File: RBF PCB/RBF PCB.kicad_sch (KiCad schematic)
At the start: 0 parts

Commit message: schematic finished
schematic is finished and pending review
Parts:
- added J1, J2, J5, J6: DF11-12DP, Connector_Hirose:Hirose_DF11-12DP-2DSA_2x06_P2.00mm_Vertical, symbol Connector_Generic:Conn_02x06_Odd_Even
- added J3, J4, J7, J8: Conn_01x04_Pin, Connector_PinSocket_2.54mm:PinSocket_1x04_P2.54mm_Vertical, symbol Connector:Conn_01x04_Pin
- added J9: B2B-XH-A, DF-11:JST_B2B-XH-A, symbol DF-11:B2B-XH-A
- added SW1: (no value), FOOT print libary:RBF Switch foot print, symbol New_Library:RBF_swtich
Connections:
- new net +3V3: J1.11 (Pin_11), J2.11 (Pin_11), J3.4 (Pin_4), J4.4 (Pin_4), J5.11 (Pin_11), J6.11 (Pin_11), J7.4 (Pin_4), J8.4 (Pin_4)
- new net GND: J1.2 (Pin_2), J1.4 (Pin_4), J1.6 (Pin_6), J1.8 (Pin_8), J2.2 (Pin_2), J2.4 (Pin_4), J2.6 (Pin_6), J2.8 (Pin_8), J3.1 (Pin_1), J4.1 (Pin_1), J5.2 (Pin_2), J5.4 (Pin_4), J5.6 (Pin_6), J5.8 (Pin_8), J6.2 (Pin_2), J6.4 (Pin_4), J6.6 (Pin_6), J6.8 (Pin_8), J7.1 (Pin_1), J8.1 (Pin_1), J9.2
- new net NC: J1.1 (Pin_1), J1.3 (Pin_3), J1.5 (Pin_5), J1.7 (Pin_7), J1.9 (Pin_9), J2.1 (Pin_1), J2.3 (Pin_3), J2.5 (Pin_5), J2.7 (Pin_7), J2.9 (Pin_9), J5.1 (Pin_1), J5.3 (Pin_3), J5.5 (Pin_5), J5.7 (Pin_7), J5.9 (Pin_9), J6.1 (Pin_1), J6.3 (Pin_3), J6.5 (Pin_5), J6.7 (Pin_7), J6.9 (Pin_9), J9.1, SW1.1 (COM), SW1.3 (NC)
- new net SCL_IN1: J1.12 (Pin_12), J3.3 (Pin_3), J5.12 (Pin_12), J7.3 (Pin_3)
- new net SCL_IN2: J2.12 (Pin_12), J4.3 (Pin_3), J6.12 (Pin_12), J8.3 (Pin_3)
- new net SDA_IN1: J1.10 (Pin_10), J3.2 (Pin_2), J5.10 (Pin_10), J7.2 (Pin_2)
- new net SDA_IN2: J2.10 (Pin_10), J4.2 (Pin_2), J6.10 (Pin_10), J8.2 (Pin_2)
- no-connect marks 0 -> 1
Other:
- note added: "Battery pack in"
- note added: "Battery pack out for the power board"
- note added: "DF-11 7.5V connection for the heaters"
- note added: "RBF Switch"

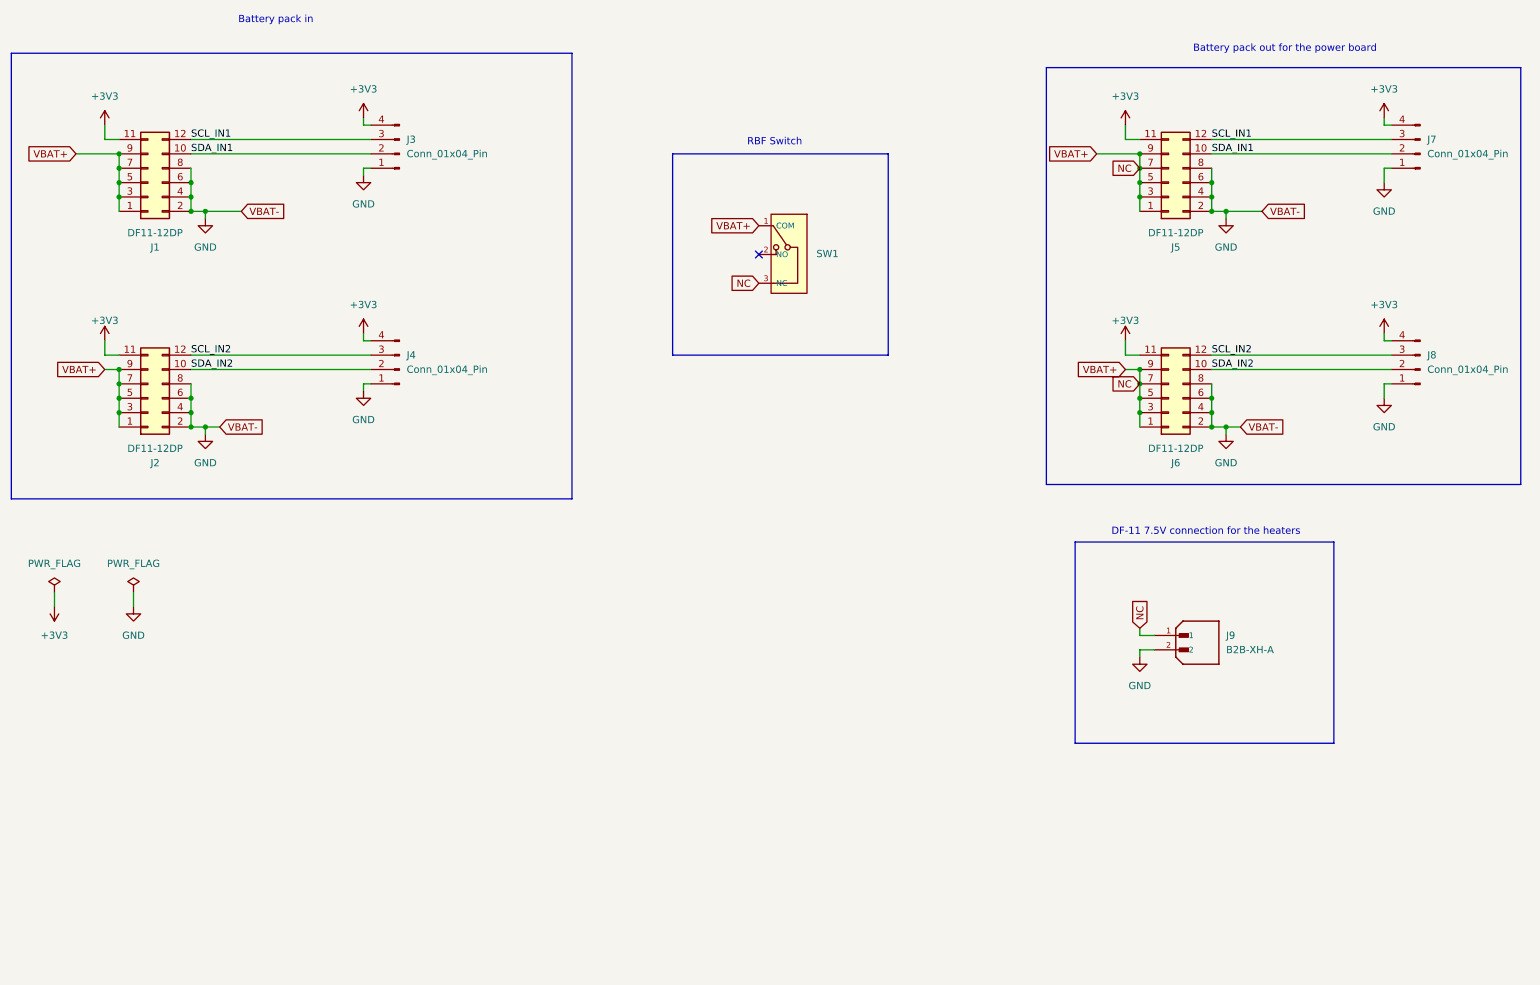
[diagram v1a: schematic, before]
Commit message: update
small revision, and added mounting holes
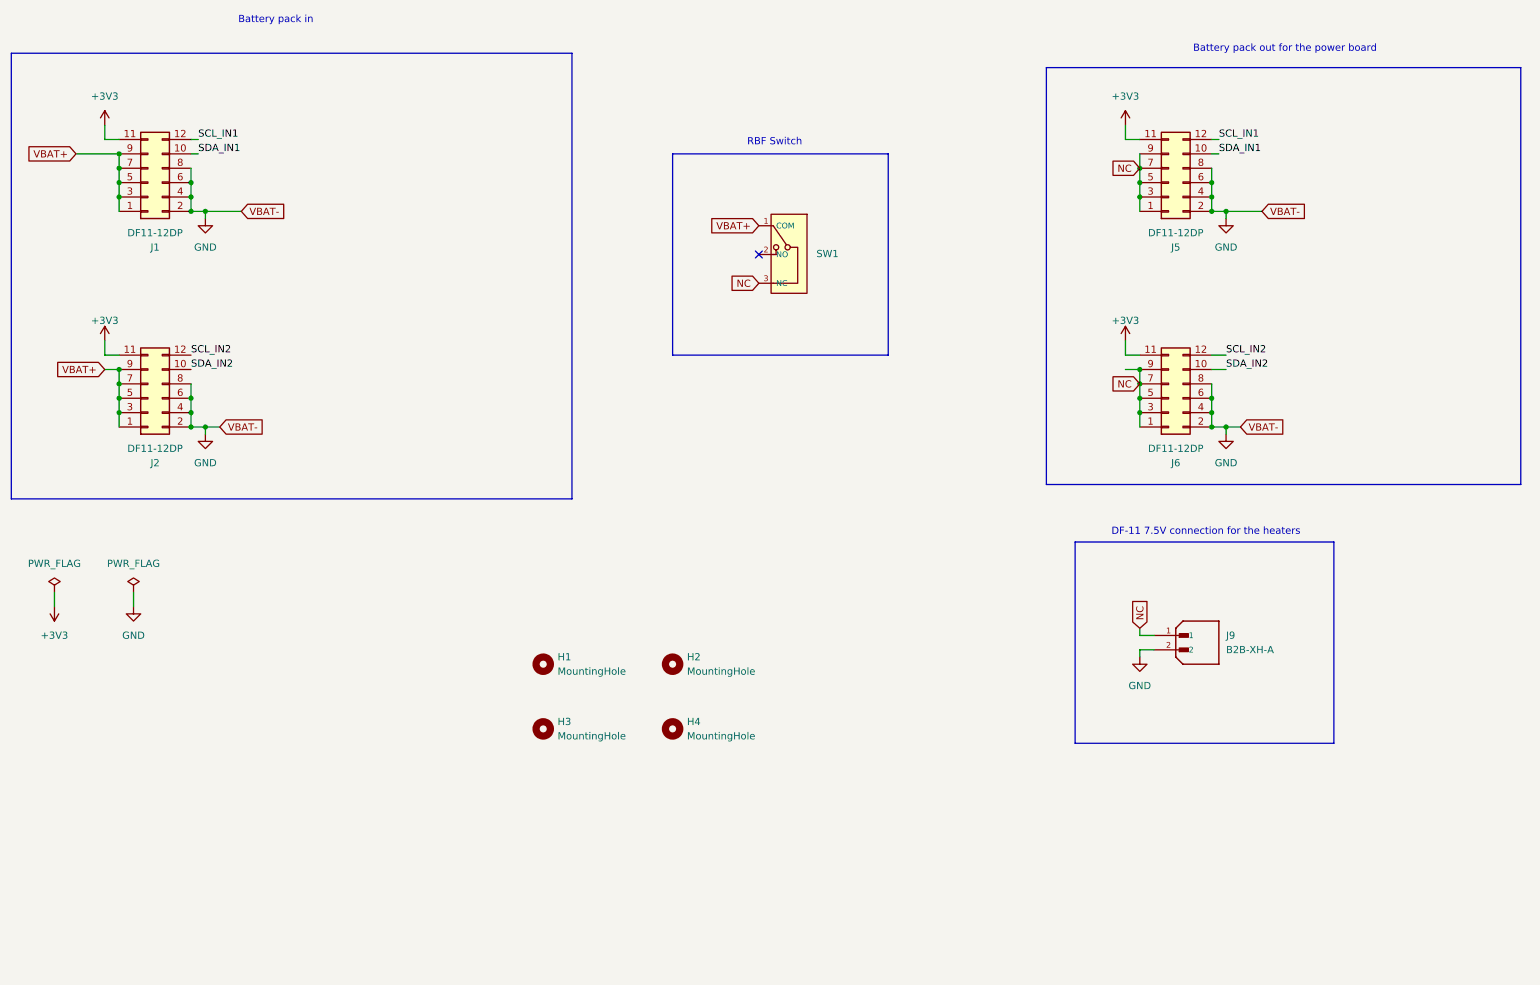
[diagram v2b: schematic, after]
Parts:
- removed J3, J4, J7, J8: Conn_01x04_Pin, Connector_PinSocket_2.54mm:PinSocket_1x04_P2.54mm_Vertical, symbol Connector:Conn_01x04_Pin
- added H1, H2, H3, H4: MountingHole, MountingHole:MountingHole_2.7mm_M2.5_Pad_Via, symbol Mechanical:MountingHole
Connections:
- net NC: no longer J1.1 (Pin_1), J1.3 (Pin_3), J1.5 (Pin_5), J1.7 (Pin_7), J1.9 (Pin_9), J2.1 (Pin_1), J2.3 (Pin_3), J2.5 (Pin_5), J2.7 (Pin_7), J2.9 (Pin_9), SW1.1 (COM)
- new net VBAT+: J1.1 (Pin_1), J1.3 (Pin_3), J1.5 (Pin_5), J1.7 (Pin_7), J1.9 (Pin_9), J2.1 (Pin_1), J2.3 (Pin_3), J2.5 (Pin_5), J2.7 (Pin_7), J2.9 (Pin_9), SW1.1 (COM)

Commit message: finial push before revision
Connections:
- removed net +3V3: J1.11 (Pin_11), J2.11 (Pin_11), J5.11 (Pin_11), J6.11 (Pin_11)
- net SCL_IN1: no longer names the net of J5.12 (Pin_12)
- net SCL_IN1: no longer J1.12 (Pin_12)
- net SCL_IN2: no longer names the net of J6.12 (Pin_12)
- net SCL_IN2: no longer J2.12 (Pin_12)
- net SDA_IN1: no longer names the net of J5.10 (Pin_10)
- net SDA_IN1: no longer J1.10 (Pin_10)
- net SDA_IN2: no longer names the net of J6.10 (Pin_10)
- net SDA_IN2: no longer J2.10 (Pin_10)
- no-connect marks 1 -> 13
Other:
- moved on the sheet: H1, H2, H3, H4, J1, J2, J5, J6, J9, SW1

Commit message: updated mounting holes
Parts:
- H1, H2, H3, H4: footprint MountingHole:MountingHole_2.7mm_M2.5_Pad_Via -> MountingHole:MountingHole_3.2mm_M3_Pad_Via
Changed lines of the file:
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@@
 			)
 		)
-		(property "Footprint" "MountingHole:MountingHole_2.7mm_M2.5_Pad_Via"
+		(property "Footprint" "MountingHole:MountingHole_3.2mm_M3_Pad_Via"
 			(at 19.05 176.53 0)
 			(hide yes)
@@
 			)
 		)
-		(property "Footprint" "MountingHole:MountingHole_2.7mm_M2.5_Pad_Via"
+		(property "Footprint" "MountingHole:MountingHole_3.2mm_M3_Pad_Via"
 			(at 19.05 187.96 0)
 			(hide yes)
@@
 			)
 		)
-		(property "Footprint" "MountingHole:MountingHole_2.7mm_M2.5_Pad_Via"
+		(property "Footprint" "MountingHole:MountingHole_3.2mm_M3_Pad_Via"
 			(at 41.91 176.53 0)
 			(hide yes)
@@
 			)
 		)
-		(property "Footprint" "MountingHole:MountingHole_2.7mm_M2.5_Pad_Via"
+		(property "Footprint" "MountingHole:MountingHole_3.2mm_M3_Pad_Via"
 			(at 41.91 187.96 0)
 			(hide yes)

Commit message: .
.
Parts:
- H1, H2, H3, H4: footprint MountingHole:MountingHole_3.2mm_M3_Pad_Via -> MountingHole:MountingHole_2.7mm_M2.5_Pad_Via
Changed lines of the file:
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@@
 			)
 		)
-		(property "Footprint" "MountingHole:MountingHole_3.2mm_M3_Pad_Via"
+		(property "Footprint" "MountingHole:MountingHole_2.7mm_M2.5_Pad_Via"
 			(at 19.05 176.53 0)
 			(hide yes)
@@
 			)
 		)
-		(property "Footprint" "MountingHole:MountingHole_3.2mm_M3_Pad_Via"
+		(property "Footprint" "MountingHole:MountingHole_2.7mm_M2.5_Pad_Via"
 			(at 19.05 187.96 0)
 			(hide yes)
@@
 			)
 		)
-		(property "Footprint" "MountingHole:MountingHole_3.2mm_M3_Pad_Via"
+		(property "Footprint" "MountingHole:MountingHole_2.7mm_M2.5_Pad_Via"
 			(at 41.91 176.53 0)
 			(hide yes)
@@
 			)
 		)
-		(property "Footprint" "MountingHole:MountingHole_3.2mm_M3_Pad_Via"
+		(property "Footprint" "MountingHole:MountingHole_2.7mm_M2.5_Pad_Via"
 			(at 41.91 187.96 0)
 			(hide yes)
